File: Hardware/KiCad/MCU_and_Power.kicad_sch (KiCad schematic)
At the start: 43 parts

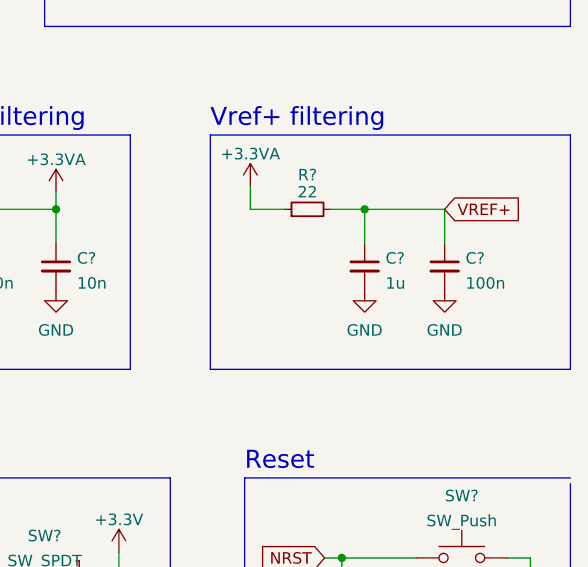
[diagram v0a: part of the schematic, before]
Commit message: Added more footprints
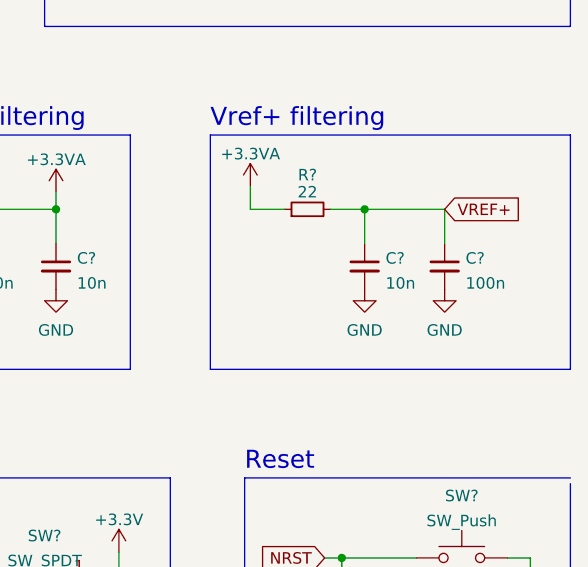
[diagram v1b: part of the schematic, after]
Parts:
- C? (x20): footprint (none) -> Capacitor_SMD:C_0402_1005Metric
- C? (x3): footprint (none) -> Capacitor_SMD:C_0603_1608Metric
- C?: value 1u -> 10n; footprint (none) -> Capacitor_SMD:C_0402_1005Metric
- FB? (x2): footprint (none) -> Inductor_SMD:L_0603_1608Metric
- R? (x12): footprint (none) -> Resistor_SMD:R_0402_1005Metric

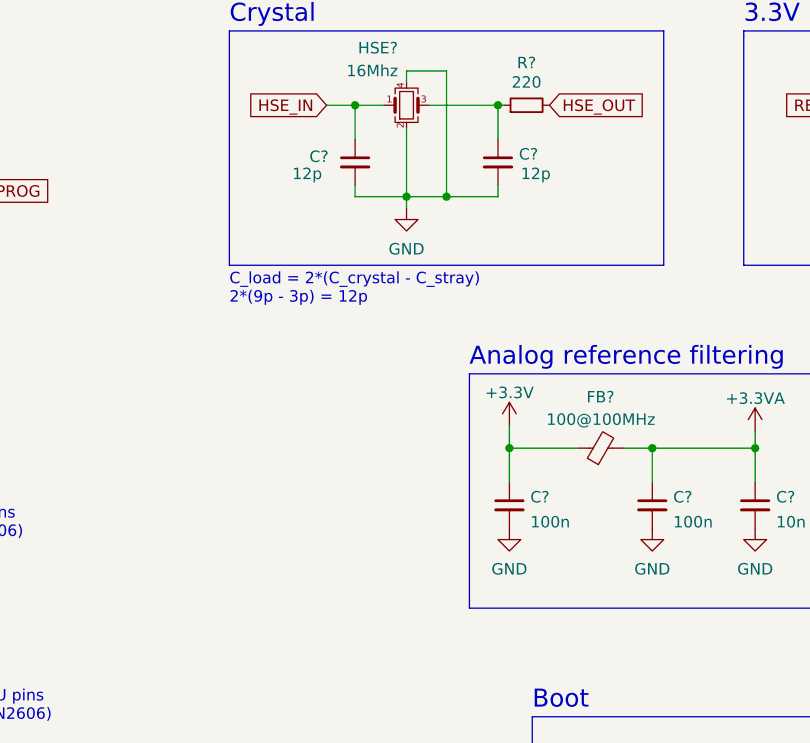
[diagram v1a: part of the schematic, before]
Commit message: added all footprints and reorganized schematic
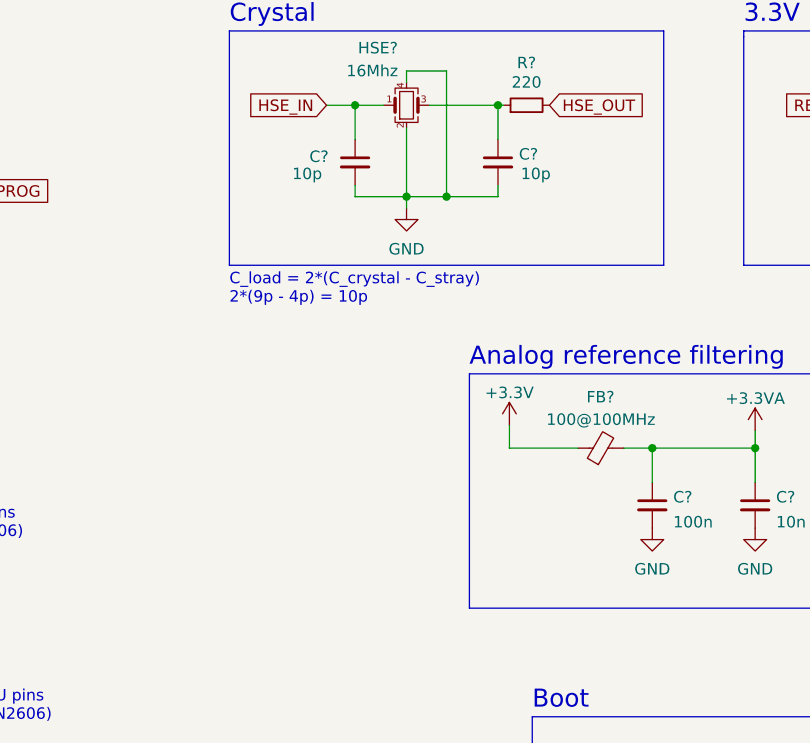
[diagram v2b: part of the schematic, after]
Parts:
- removed C?: 100n, Capacitor_SMD:C_0402_1005Metric, symbol Device:C_Small
- C? (x2): value 12p -> 10p
- SW?: footprint (none) -> Button_Switch_SMD:SW_SPDT_PCM12
- SW?: footprint (none) -> Button_Switch_SMD:SW_SPST_FSMSM
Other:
- note added: "C_load = 2*(C_crystal - C_stray) 2*(9p - 4p) = 10p"
- note removed: "C_load = 2*(C_crystal - C_stray) 2*(9p - 3p) = 12p"
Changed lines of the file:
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@@
   (junction (at 215.9 27.94) (diameter 0) (color 0 0 0 0)
-  )
-  (junction (at 189.865 101.6) (diameter 0) (color 0 0 0 0)
   )
   (junction (at 264.16 63.5) (diameter 0) (color 0 0 0 0)
@@
   )
   (polyline (pts (xy 229.87 157.48) (xy 192.405 157.48))
-    (stroke (width 0) (type default) (color 0 0 0 0))
-  )
-  (wire (pts (xy 189.865 101.6) (xy 189.865 105.41))
     (stroke (width 0) (type default) (color 0 0 0 0))
   )
@@
     (effects (font (size 1.27 1.27)) (justify left bottom))
   )
-  (text "C_load = 2*(C_crystal - C_stray) \n2*(9p - 3p) = 12p"
+  (text "C_load = 2*(C_crystal - C_stray) \n2*(9p - 4p) = 10p"
     (at 158.75 85.725 0)
     (effects (font (size 1.27 1.27)) (justify left bottom))
@@
     (property "Reference" "SW?" (id 0) (at 215.9 137.8925 0))
     (property "Value" "SW_SPDT" (id 1) (at 215.9 140.6676 0))
-    (property "Footprint" "" (id 2) (at 215.9 144.78 0)
-      (effects (font (size 1.27 1.27)) hide)
-    )
-    (property "Datasheet" "~" (id 3) (at 215.9 144.78 0)
+    (property "Footprint" "Button_Switch_SMD:SW_SPDT_PCM12" (id 2) (at 215.9 144.78 0)
+      (effects (font (size 1.27 1.27)) hide)
+    )
+    (property "Datasheet" "https://datasheet.lcsc.com/lcsc/1808041445_ALPSALPINE-SSSS811101_C109335.pdf" (id 3) (at 215.9 144.78 0)
       (effects (font (size 1.27 1.27)) hide)
     )
@@
     (pin "2")
   )
-  (symbol (lib_id "Device:C_Small") (at 189.865 107.95 0) (unit 1)
-    (in_bom yes) (on_board yes) (fields_autoplaced)
-    (property "Reference" "C?" (id 0) (at 192.1891 107.0478 0)
-      (effects (font (size 1.27 1.27)) (justify left))
-    )
-    (property "Value" "100n" (id 1) (at 192.1891 109.8229 0)
-      (effects (font (size 1.27 1.27)) (justify left))
-    )
-    (property "Footprint" "Capacitor_SMD:C_0402_1005Metric" (id 2) (at 189.865 107.95 0)
-      (effects (font (size 1.27 1.27)) hide)
-    )
-    (property "Datasheet" "~" (id 3) (at 189.865 107.95 0)
-      (effects (font (size 1.27 1.27)) hide)
-    )
-    (pin "1")
-    (pin "2")
-  )
-  (symbol (lib_id "power:GND") (at 189.865 110.49 0) (unit 1)
-    (in_bom yes) (on_board yes) (fields_autoplaced)
-    (property "Reference" "#PWR0119" (id 0) (at 189.865 116.84 0)
-      (effects (font (size 1.27 1.27)) hide)
-    )
-    (property "Value" "GND" (id 1) (at 189.865 115.0525 0))
-    (property "Footprint" "" (id 2) (at 189.865 110.49 0)
-      (effects (font (size 1.27 1.27)) hide)
-    )
-    (property "Datasheet" "" (id 3) (at 189.865 110.49 0)
-      (effects (font (size 1.27 1.27)) hide)
-    )
-    (pin "1")
-  )
   (symbol (lib_id "Device:R_Small") (at 111.76 156.845 90) (unit 1)
     (in_bom yes) (on_board yes)
@@
       (effects (font (size 1.27 1.27)) (justify left))
     )
-    (property "Value" "12p" (id 1) (at 191.135 71.12 0)
+    (property "Value" "10p" (id 1) (at 191.135 71.12 0)
       (effects (font (size 1.27 1.27)) (justify left))
     )
@@
       (effects (font (size 1.27 1.27)) (justify left))
     )
-    (property "Value" "12p" (id 1) (at 165.735 71.12 0)
+    (property "Value" "10p" (id 1) (at 165.735 71.12 0)
       (effects (font (size 1.27 1.27)) (justify left))
     )
@@
     (property "Reference" "SW?" (id 0) (at 262.255 133.4475 0))
     (property "Value" "SW_Push" (id 1) (at 262.255 136.2226 0))
-    (property "Footprint" "" (id 2) (at 262.255 135.255 0)
-      (effects (font (size 1.27 1.27)) hide)
-    )
+    (property "Footprint" "Button_Switch_SMD:SW_SPST_FSMSM" (id 2) (at 262.255 135.255 0)
+      (effects (font (size 1.27 1.27)) hide)
+    )

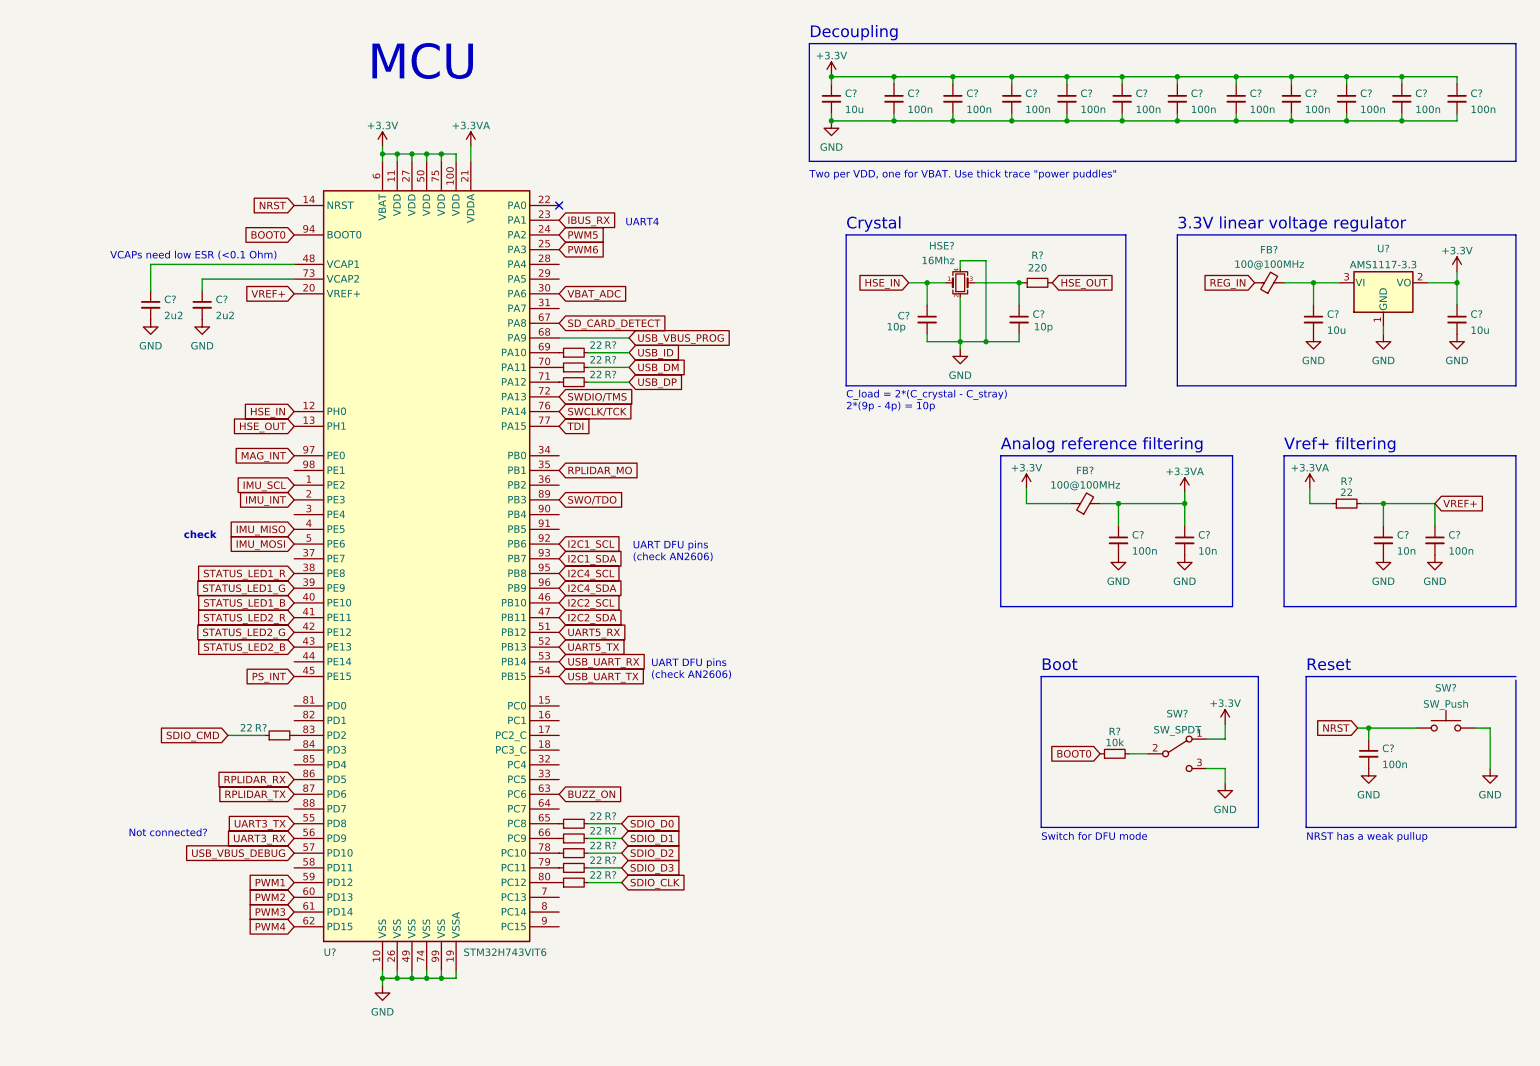
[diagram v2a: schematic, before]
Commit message: Added more current limiting resistors
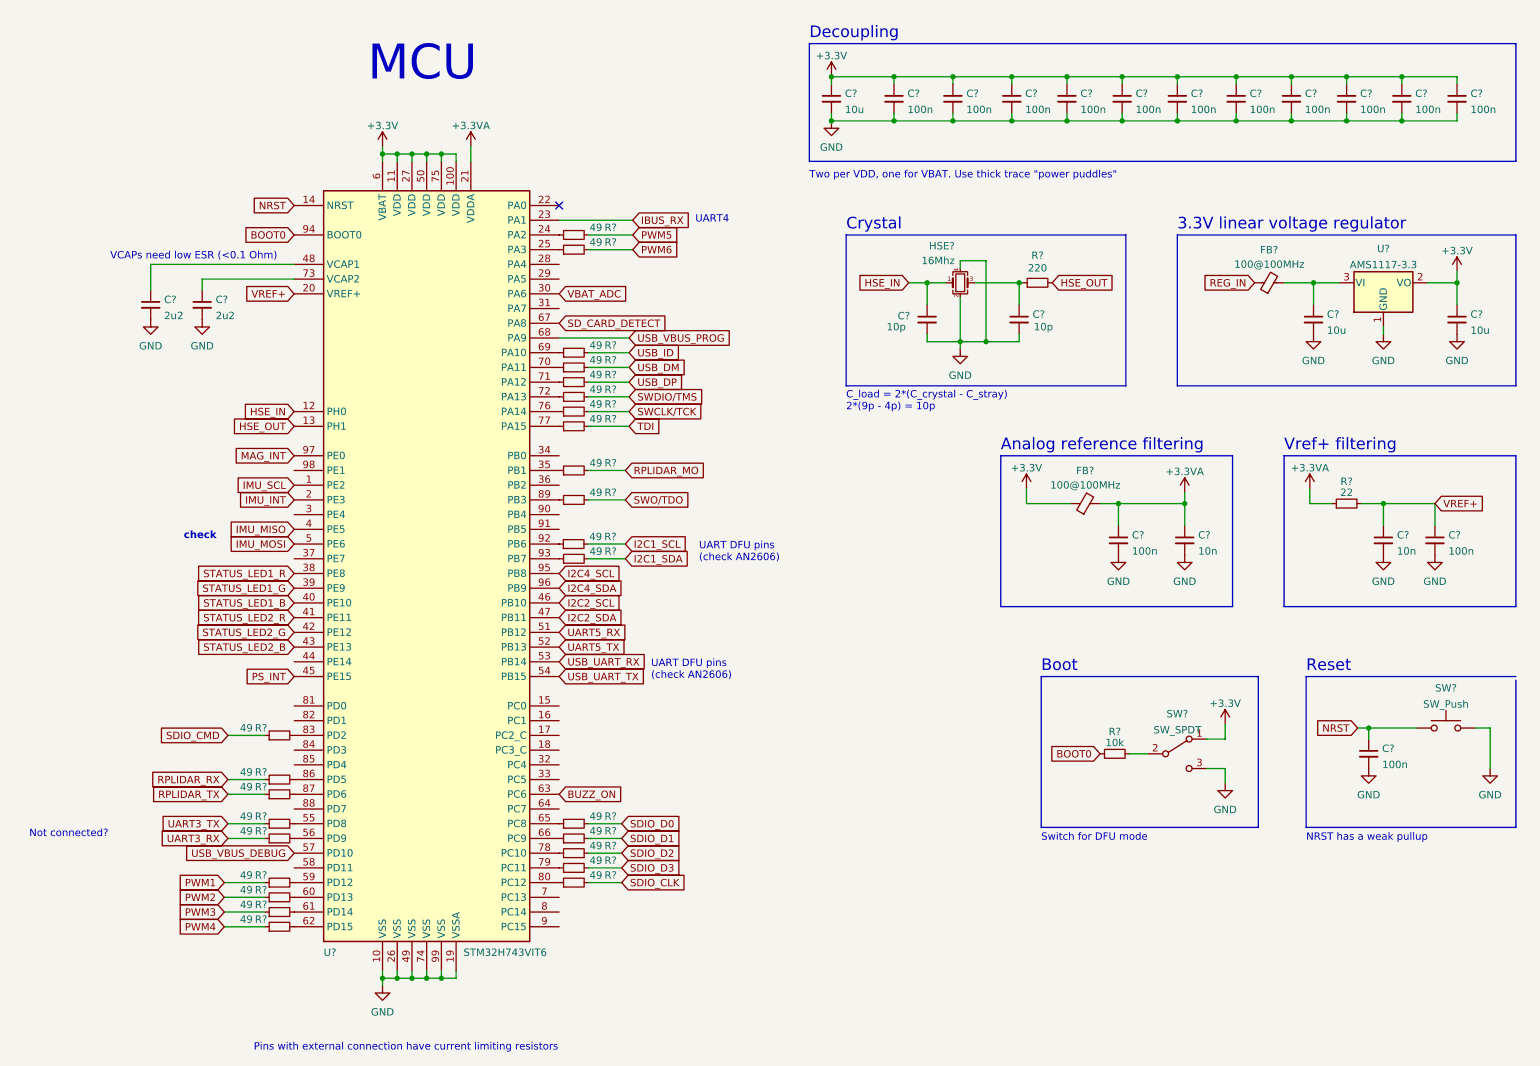
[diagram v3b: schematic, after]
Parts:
- added R? (x17): 49, Resistor_SMD:R_0402_1005Metric, symbol Device:R_Small
- R? (x9): value 22 -> 49
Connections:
- net I2C1_SCL: now also R?.2; no longer U?.92 (PB6)
- net I2C1_SDA: now also R?.2; no longer U?.93 (PB7)
- net PWM1: now also R?.1; no longer U?.59 (PD12)
- net PWM2: now also R?.1; no longer U?.60 (PD13)
- net PWM3: now also R?.1; no longer U?.61 (PD14)
- net PWM4: now also R?.1; no longer U?.62 (PD15)
- net PWM5: now also R?.2; no longer U?.24 (PA2)
- net PWM6: now also R?.2; no longer U?.25 (PA3)
- net RPLIDAR_MO: now also R?.2; no longer U?.35 (PB1)
- net RPLIDAR_RX: now also R?.1; no longer U?.86 (PD5)
- net RPLIDAR_TX: now also R?.1; no longer U?.87 (PD6)
- net SWCLK/TCK: now also R?.2; no longer U?.76 (PA14)
- net SWDIO/TMS: now also R?.2; no longer U?.72 (PA13)
- net SWO/TDO: now also R?.2; no longer U?.89 (PB3)
- net TDI: now also R?.2; no longer U?.77 (PA15)
- net UART3_RX: now also R?.1; no longer U?.56 (PD9)
- net UART3_TX: now also R?.1; no longer U?.55 (PD8)
- new net: R?.1, U?.77 (PA15)
- new net: R?.1, U?.25 (PA3)
- new net: R?.1, U?.24 (PA2)
- new net: R?.2, U?.86 (PD5)
- new net: R?.2, U?.62 (PD15)
- new net: R?.1, U?.76 (PA14)
- new net: R?.1, U?.35 (PB1)
- new net: R?.2, U?.55 (PD8)
- new net: R?.2, U?.56 (PD9)
- new net: R?.2, U?.59 (PD12)
- new net: R?.2, U?.60 (PD13)
- new net: R?.2, U?.61 (PD14)
- new net: R?.1, U?.72 (PA13)
- new net: R?.2, U?.87 (PD6)
- new net: R?.1, U?.89 (PB3)
- new net: R?.1, U?.93 (PB7)
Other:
- note added: "Pins with external connection have current limiting resistors"

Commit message: Changed supply voltage for CH330N 5V->3V3
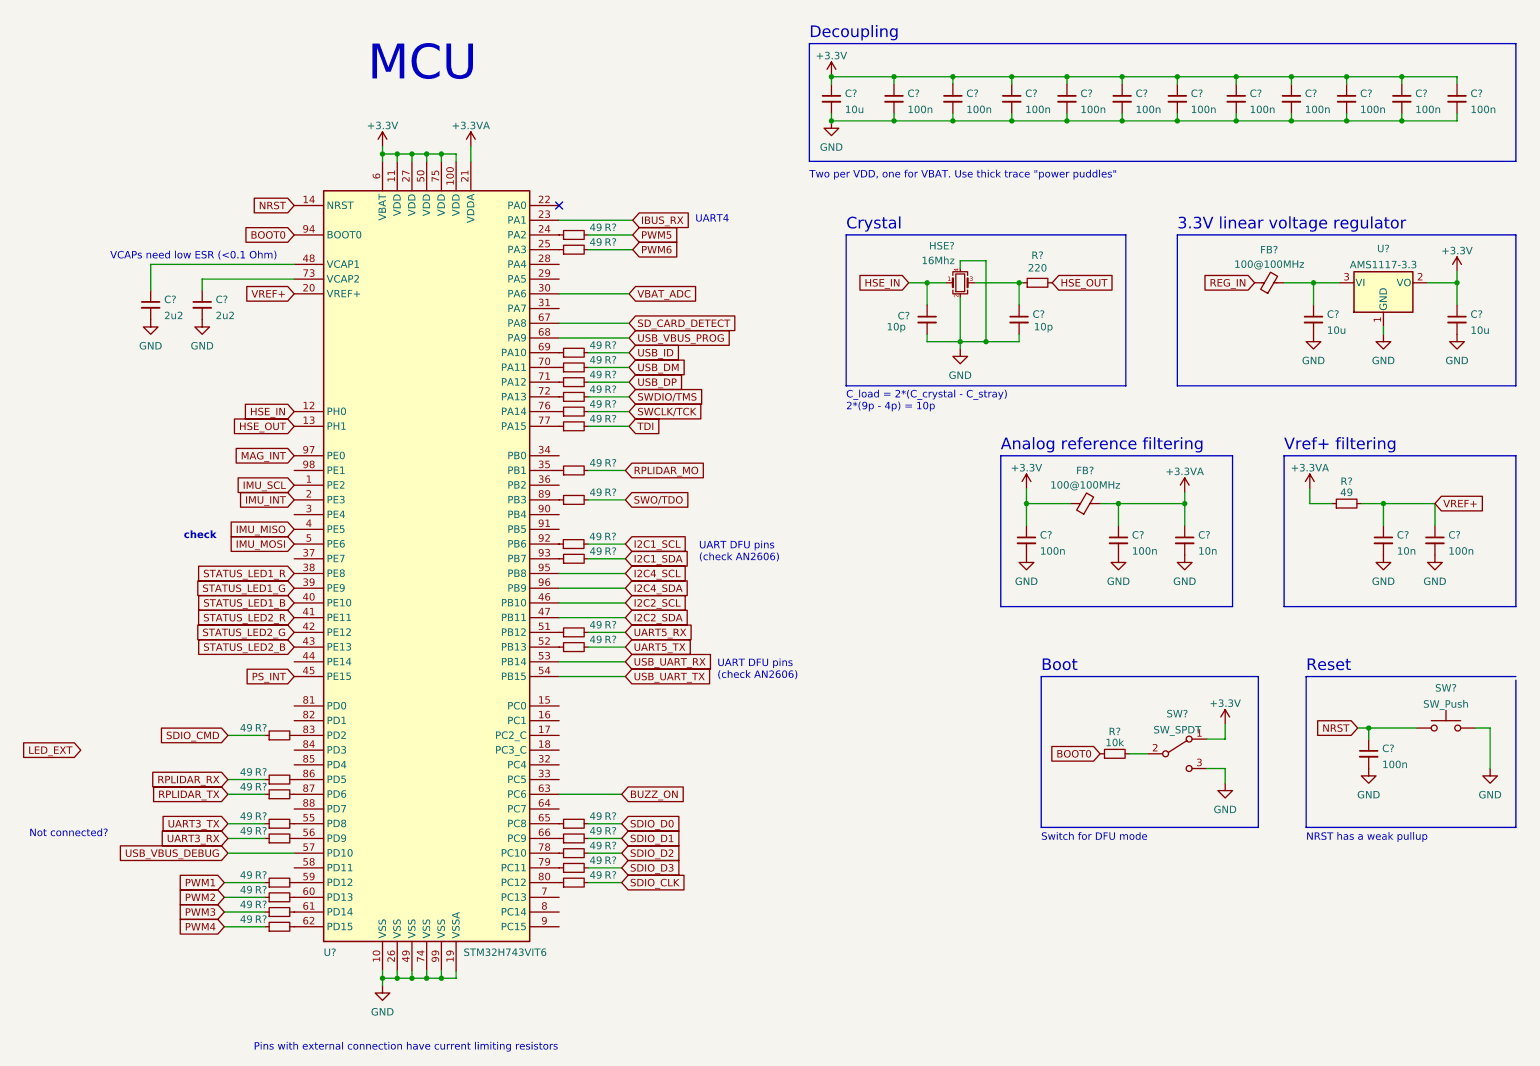
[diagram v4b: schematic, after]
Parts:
- added C?: 100n, Capacitor_SMD:C_0402_1005Metric, symbol Device:C_Small
- added R? (x2): 49, Resistor_SMD:R_0402_1005Metric, symbol Device:R_Small
- R?: value 22 -> 49
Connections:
- net +3V3: now also C?.1
- net GND: now also C?.2
- net UART5_RX: now also R?.2; no longer U?.51 (PB12)
- net UART5_TX: now also R?.2; no longer U?.52 (PB13)
- new net: R?.1, U?.52 (PB13)
- new net: R?.1, U?.51 (PB12)
